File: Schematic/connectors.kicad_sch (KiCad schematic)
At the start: 31 parts, among them J11 PIN2216, J12 PIN2216, J2 PIN2216, J3 PIN2216, J4 PIN2216, J5 PIN2216, J6 PIN2216, J7 PIN2216, J8 PIN2216, J9 PIN2216, U10 HDGC1002WR-S-4P, U11 HDGC1002WR-S-4P, U14 HDGC1002WR-S-4P, U15 HDGC1002WR-S-6P, U16 HDGC1002WR-S-8P, U17 HDGC1002WR-S-8P, U7 HDGC1002WR-S-4P, U8 HDGC1002WR-S-4P, U9 HDGC1002WR-S-4P

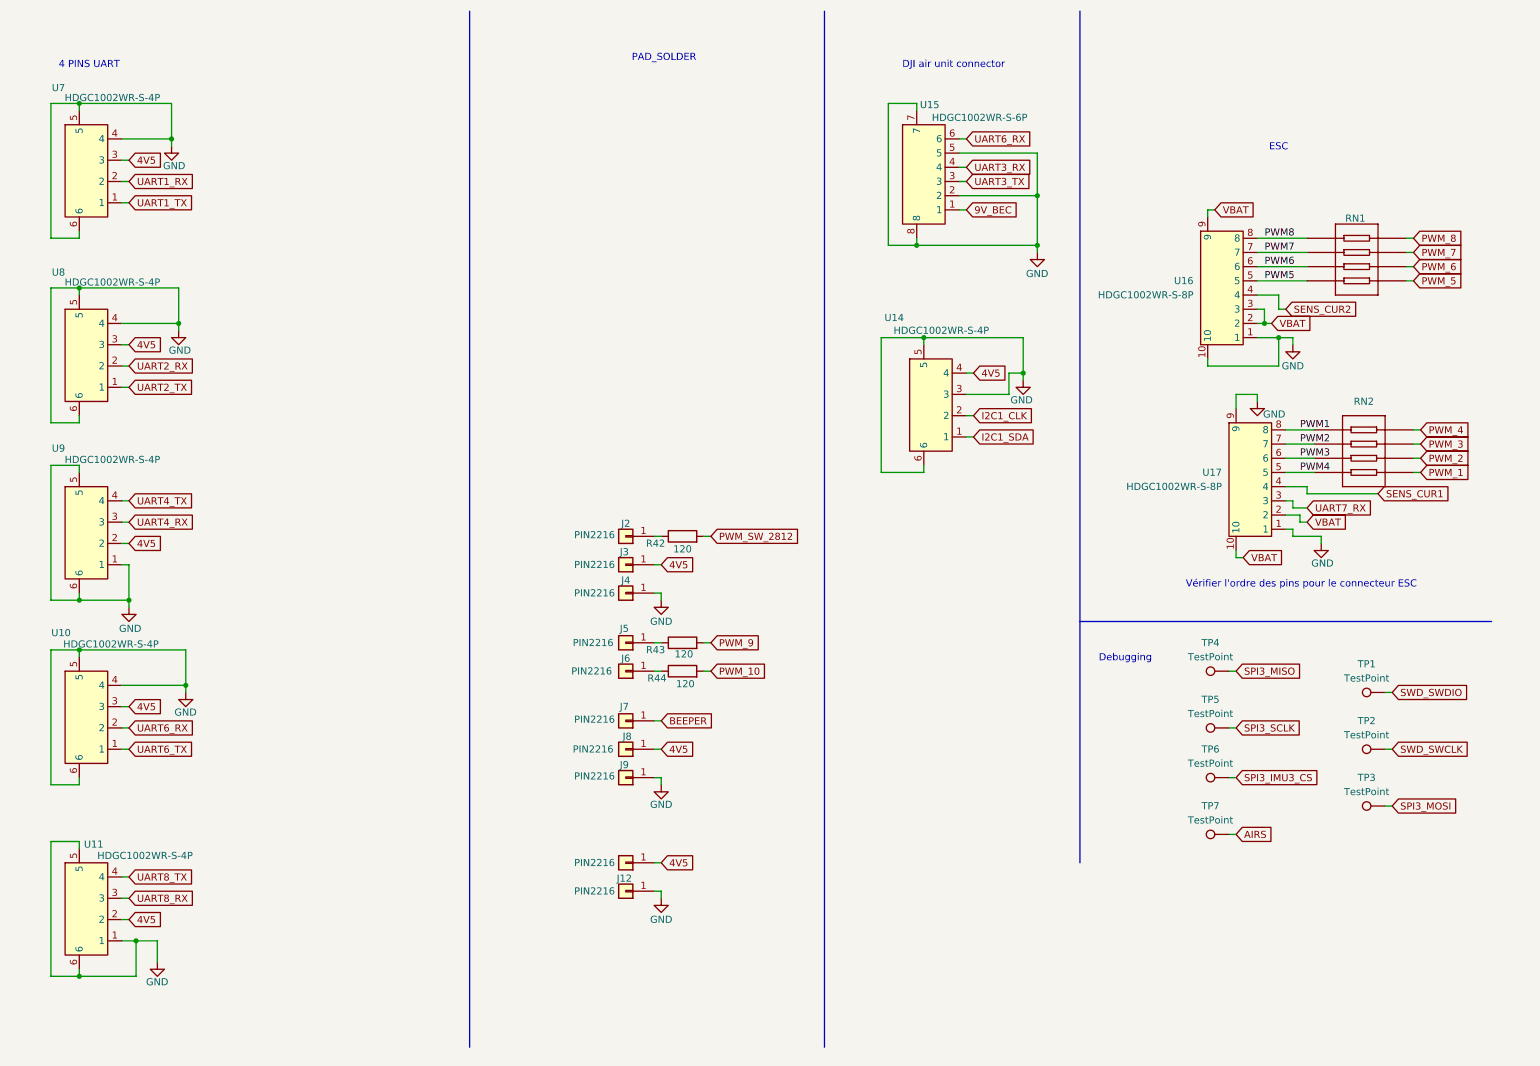
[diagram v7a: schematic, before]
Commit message: optimisation : - refactoring two 4 pin connector for mag and gps into one 6 pin connector - increased output voltage from 5V buck regulator to take into account voltage decrease schottky diodes
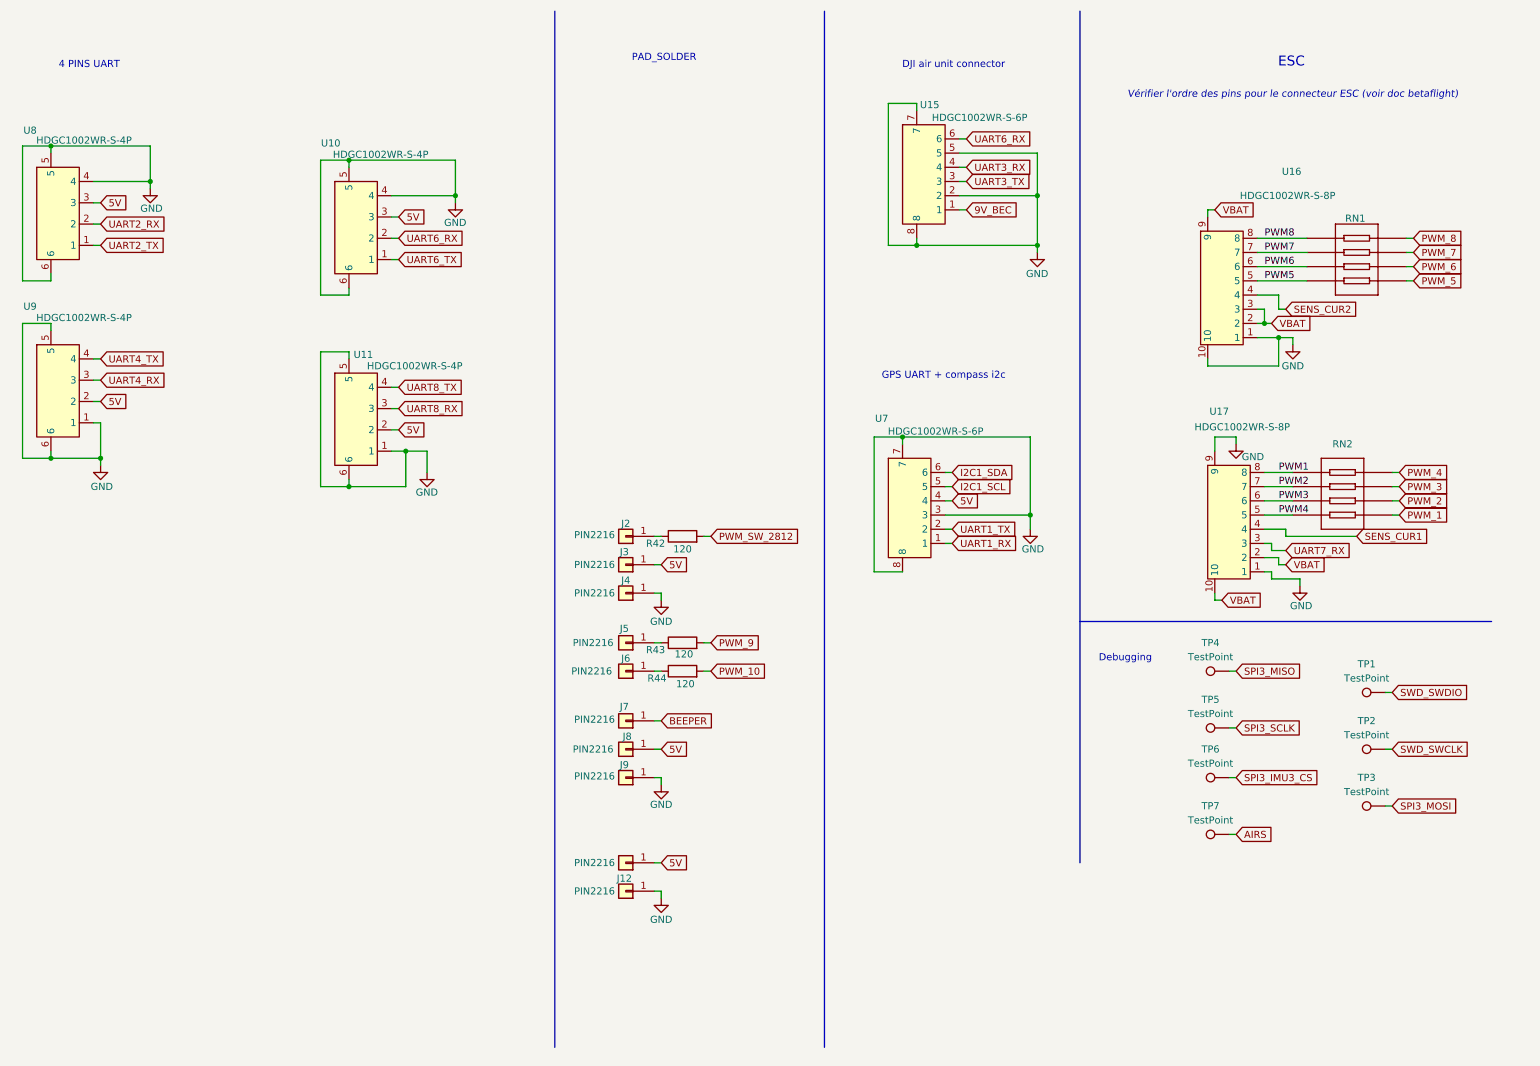
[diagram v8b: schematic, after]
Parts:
- removed U14, U7: HDGC1002WR-S-4P, fch7:CONN-SMD_4P-P1.00_HDGC_HDGC1002WR-S-4P, symbol fclib:HDGC1002WR-S-4P
- added U7: HDGC1002WR-S-6P, fch7:CONN-SMD_HDGC1002WR-S-6P, symbol fclib:HDGC1002WR-S-6P
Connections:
- net GND: now also U7.3, U7.7, U7.8
- net I2C1_SDA: now also U7.6
- net UART1_RX: now also U7.1
- net UART1_TX: now also U7.2
- net 4V5 renamed 5V
- net 5V: now also U7.4
- new net I2C1_SCL: U7.5
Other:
- note added: "GPS UART + compass i2c"
- note added: "Vérifier l'ordre des pins pour le connecteur ESC (voir doc betaflight)"
- note removed: "Vérifier l'ordre des pins pour le connecteur ESC"
- moved on the sheet: RN2, U10, U11, U17, U8, U9
